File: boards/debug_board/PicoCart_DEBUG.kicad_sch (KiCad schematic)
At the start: 27 parts, among them J1 D_DEBUG, J2 Micro_SD_Card, J3 UART, J4 DEBUG, J5 MSX Debug, J6 D_UART, J7 Ground Pins, J8 Ground Pins, J9 DEBUG_I2C, U1 LD1117S33TR_SOT223, U2 74LS245, U3 74LS245, U4 74LS245, U6 Pico, U8 Pico

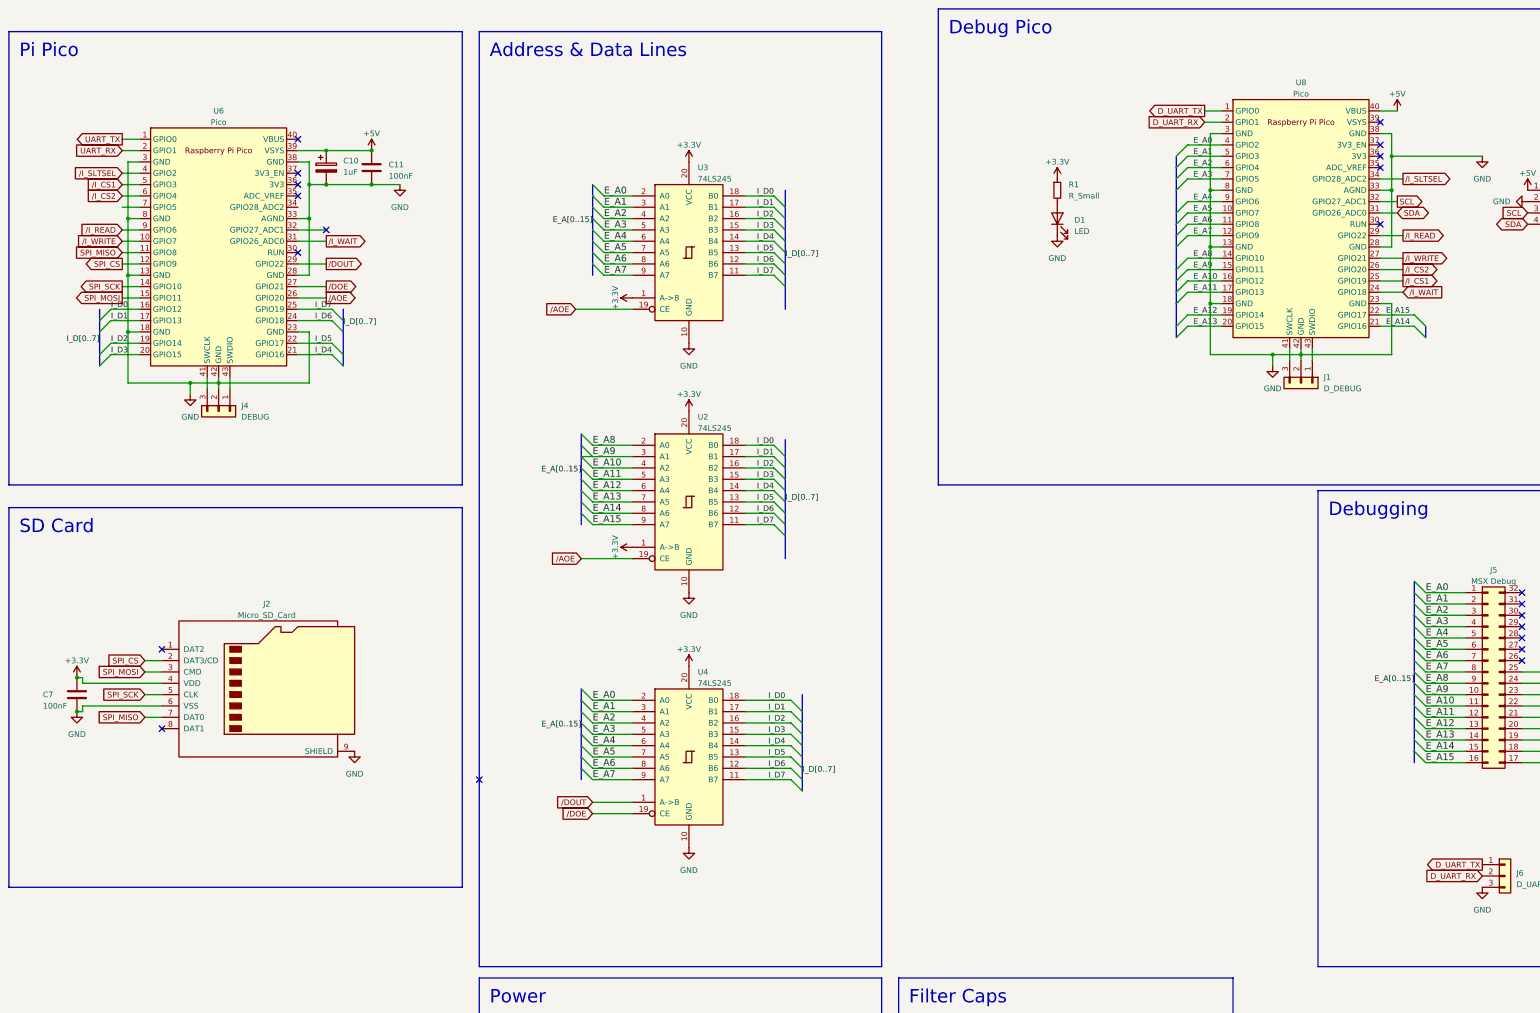
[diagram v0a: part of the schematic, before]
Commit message: Fixed circuit - last design would not have worked
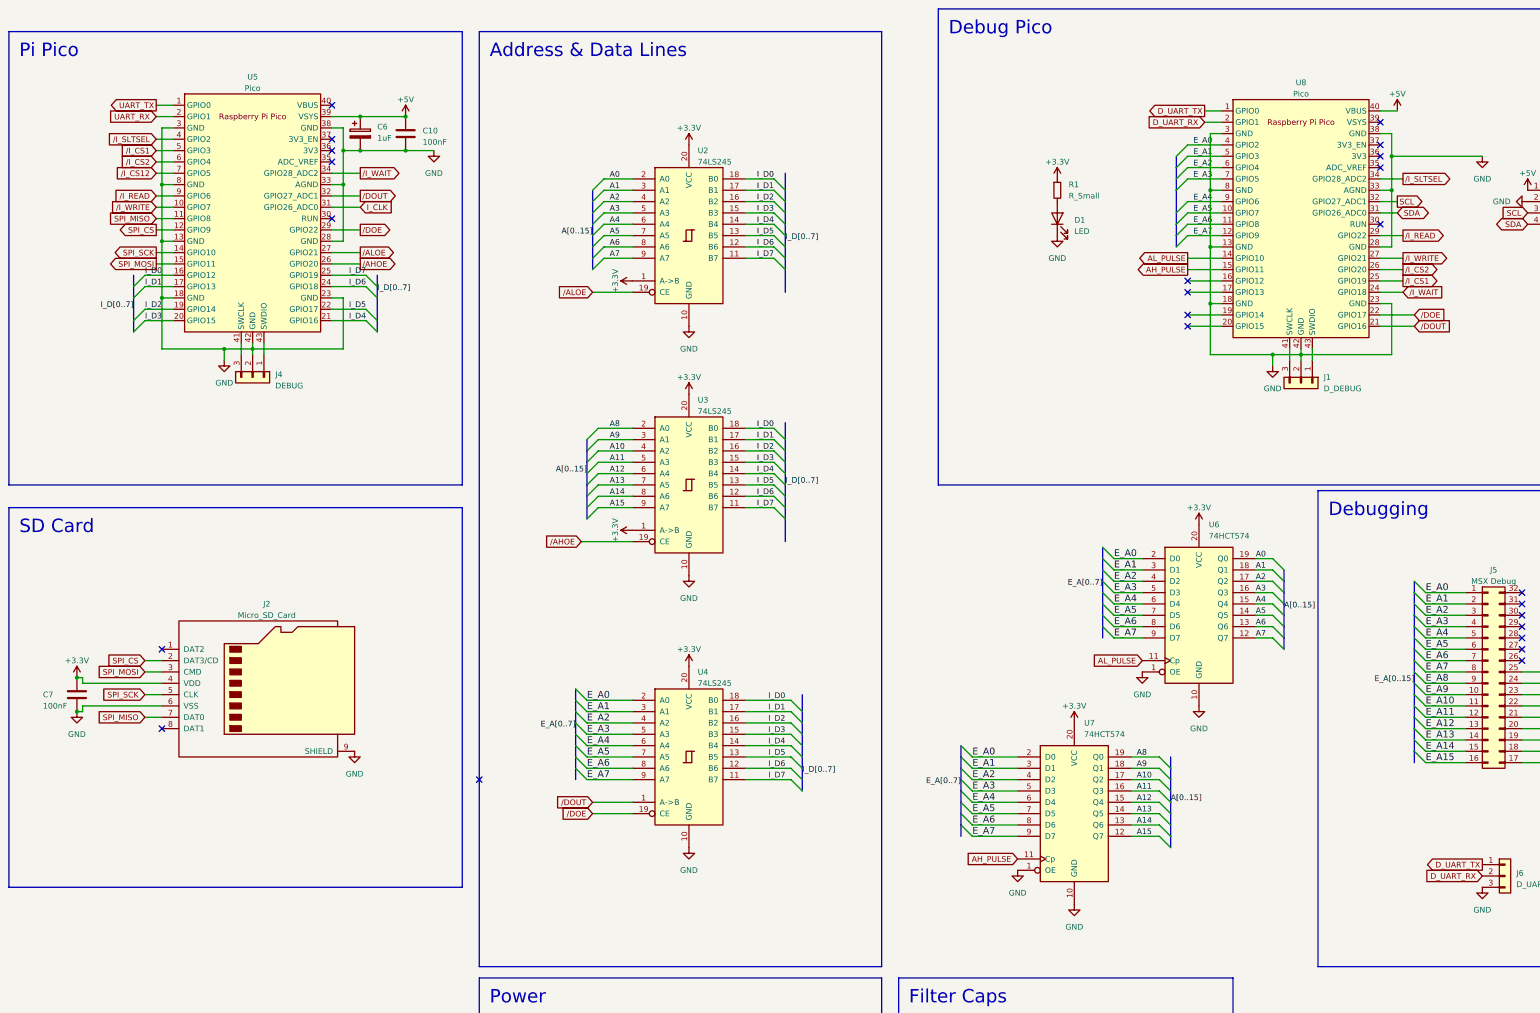
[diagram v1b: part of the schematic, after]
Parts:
- removed C10: 1uF, Capacitor_THT:CP_Radial_D5.0mm_P2.50mm, symbol Device:C_Polarized
- removed C11: 100nF, Capacitor_THT:C_Disc_D4.3mm_W1.9mm_P5.00mm, symbol Device:C
- removed U6: Pico, PicoCartLibrary:RPi_Pico_SMD_TH, symbol MCU_RaspberryPi_and_Boards:Pico
- added C10: 100nF, Capacitor_THT:C_Disc_D4.3mm_W1.9mm_P5.00mm, symbol Device:C
- added C6: 1uF, Capacitor_THT:CP_Radial_D5.0mm_P2.50mm, symbol Device:C_Polarized
- added U5: Pico, PicoCartLibrary:RPi_Pico_SMD_TH, symbol MCU_RaspberryPi_and_Boards:Pico
- added U6, U7: 74HCT574, Package_DIP:DIP-20_W7.62mm_Socket_LongPads, symbol 74xx:74HCT574
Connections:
- net +3.3V: now also U6.20 (VCC), U7.20 (VCC)
- net +5V: now also C10.1, C6.1, U5.39 (VSYS)
- net E_A0: now also U6.2 (D0), U7.2 (D0); no longer U3.2 (A0)
- net E_A1: now also U6.3 (D1), U7.3 (D1); no longer U3.3 (A1)
- net E_A10: no longer U2.4 (A2), U8.16 (GPIO12)
- net E_A11: no longer U2.5 (A3), U8.17 (GPIO13)
- net E_A12: no longer U2.6 (A4), U8.19 (GPIO14)
- net E_A13: no longer U2.7 (A5), U8.20 (GPIO15)
- net E_A14: no longer U2.8 (A6), U8.21 (GPIO16)
- net E_A15: no longer U2.9 (A7), U8.22 (GPIO17)
- net E_A2: now also U6.4 (D2), U7.4 (D2); no longer U3.4 (A2)
- net E_A3: now also U6.5 (D3), U7.5 (D3); no longer U3.5 (A3)
- net E_A4: now also U6.6 (D4), U7.6 (D4); no longer U3.6 (A4)
- net E_A5: now also U6.7 (D5), U7.7 (D5); no longer U3.7 (A5)
- net E_A6: now also U6.8 (D6), U7.8 (D6); no longer U3.8 (A6)
- net E_A7: now also U6.9 (D7), U7.9 (D7); no longer U3.9 (A7)
- net E_A8: no longer U2.2 (A0), U8.14 (GPIO10)
- net E_A9: no longer U2.3 (A1), U8.15 (GPIO11)
- net GND: now also C10.2, C6.2, U5.13 (GND), U5.18 (GND), U5.23 (GND), U5.28 (GND), U5.3 (GND), U5.33 (AGND), U5.38 (GND), U5.42 (GND), U5.8 (GND), U6.1 (OE), U6.10 (GND), U7.1 (OE), U7.10 (GND)
- net I_D0: now also U5.16 (GPIO12)
- net I_D1: now also U5.17 (GPIO13)
- net I_D2: now also U5.19 (GPIO14)
- net I_D3: now also U5.20 (GPIO15)
- net I_D4: now also U5.21 (GPIO16)
- net I_D5: now also U5.22 (GPIO17)
- net I_D6: now also U5.24 (GPIO18)
- net I_D7: now also U5.25 (GPIO19)
- net SPI_CS: now also U5.12 (GPIO9)
- net SPI_MISO: now also U5.11 (GPIO8)
- net SPI_MOSI: now also U5.15 (GPIO11)
- net SPI_SCK: now also U5.14 (GPIO10)
- net UART_RX: now also U5.2 (GPIO1)
- net UART_TX: now also U5.1 (GPIO0)
- net /AOE: no longer U2.19 (CE), U3.19 (CE)
- net /DOE: now also U8.22 (GPIO17), U5.29 (GPIO22)
- net /DOUT: now also U8.21 (GPIO16), U5.32 (GPIO27_ADC1)
- net /I_CS1: now also U5.5 (GPIO3)
- net /I_CS2: now also U5.6 (GPIO4)
- net /I_READ: now also U5.9 (GPIO6)
- net /I_SLTSEL: now also U5.4 (GPIO2)
- net /I_WAIT: now also U5.34 (GPIO28_ADC2)
- net /I_WRITE: now also U5.10 (GPIO7)
- net at J4.1 (Pin_1): now also U5.43 (SWDIO)
- net at J4.3 (Pin_3): now also U5.41 (SWCLK)
- new net A0: U2.2 (A0), U6.19 (Q0)
- new net A1: U2.3 (A1), U6.18 (Q1)
- new net A10: U3.4 (A2), U7.17 (Q2)
- new net A11: U3.5 (A3), U7.16 (Q3)
- new net A12: U3.6 (A4), U7.15 (Q4)
- new net A13: U3.7 (A5), U7.14 (Q5)
- new net A14: U3.8 (A6), U7.13 (Q6)
- new net A15: U3.9 (A7), U7.12 (Q7)
- new net A2: U2.4 (A2), U6.17 (Q2)
- new net A3: U2.5 (A3), U6.16 (Q3)
- new net A4: U2.6 (A4), U6.15 (Q4)
- new net A5: U2.7 (A5), U6.14 (Q5)
- new net A6: U2.8 (A6), U6.13 (Q6)
- new net A7: U2.9 (A7), U6.12 (Q7)
- new net A8: U3.2 (A0), U7.19 (Q0)
- new net A9: U3.3 (A1), U7.18 (Q1)
- new net AH_PULSE: U7.11 (Cp), U8.15 (GPIO11)
- new net AL_PULSE: U6.11 (Cp), U8.14 (GPIO10)
- new net I_CLK: U5.31 (GPIO26_ADC0)
- new net /AHOE: U3.19 (CE), U5.26 (GPIO20)
- new net /ALOE: U2.19 (CE), U5.27 (GPIO21)
- new net /I_CS12: U5.7 (GPIO5)
- no-connect marks 21 -> 24

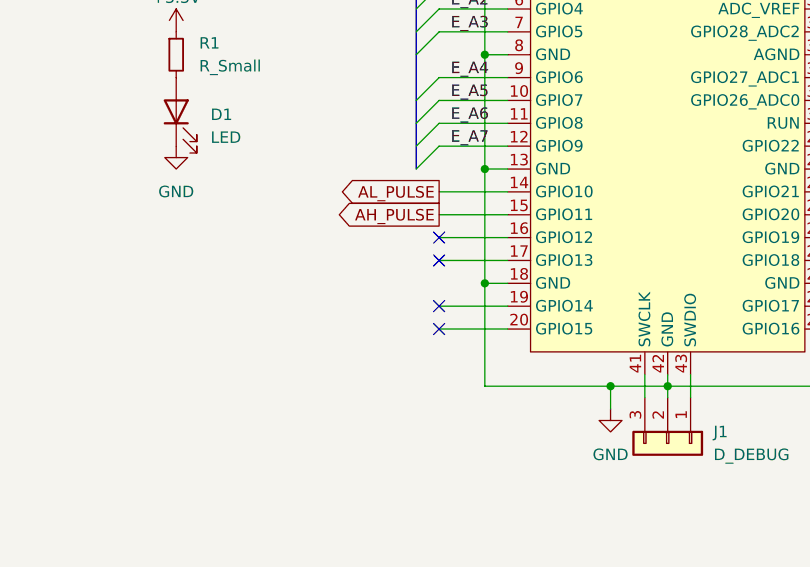
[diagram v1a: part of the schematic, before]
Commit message: Add Test Points for Spare GPIO Pins
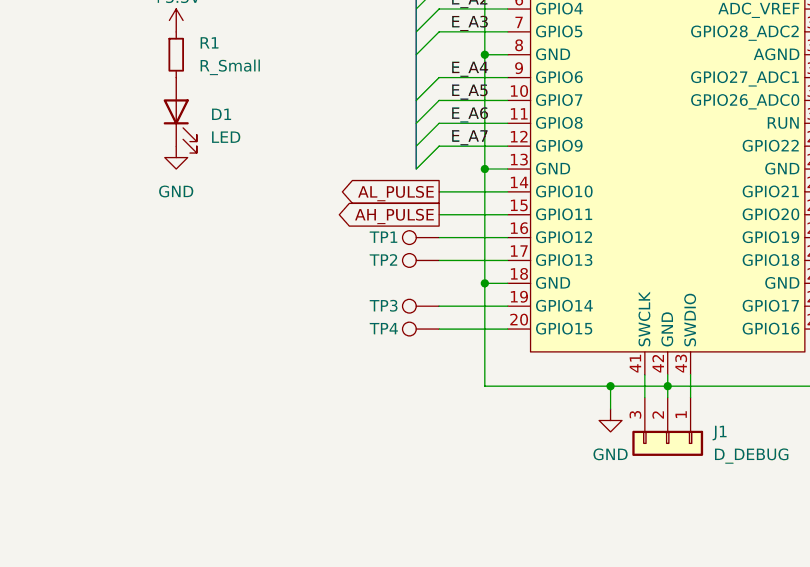
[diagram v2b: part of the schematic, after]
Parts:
- added TP1, TP2, TP3, TP4: TestPoint, TestPoint:TestPoint_Pad_D1.0mm, symbol Connector:TestPoint
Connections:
- net at U8.16 (GPIO12): now also TP1.1
- net at U8.17 (GPIO13): now also TP2.1
- net at U8.19 (GPIO14): now also TP3.1
- net at U8.20 (GPIO15): now also TP4.1
- no-connect marks 24 -> 20
